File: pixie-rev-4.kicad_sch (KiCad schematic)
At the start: 40 parts, among them J1 THD_FPC_24, SW1 SW_tact_52x52, SW2 SW_tact_52x52, SW3 SW_tact_52x52, SW4 SW_tact_52x52, U1 USBLC6-2SC6, U2 W25Q128JVS, U3 SPX3819M5-L-3-3, U4 ESP32_C3, Y2 Crystal_GND24

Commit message: Check-in before trying ESP32-C3-F4.
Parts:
- U4: footprint Package_DFN_QFN:HVQFN-32-1EP_5x5mm_P0.5mm_EP3.1x3.1mm -> Package_DFN_QFN:QFN-32-1EP_5x5mm_P0.5mm_EP3.7x3.7mm
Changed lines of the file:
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@@
       (effects (font (size 1.27 1.27)) (justify left))
     )
-    (property "Footprint" "Package_DFN_QFN:HVQFN-32-1EP_5x5mm_P0.5mm_EP3.1x3.1mm" (at 166.37 82.55 0)
+    (property "Footprint" "Package_DFN_QFN:QFN-32-1EP_5x5mm_P0.5mm_EP3.7x3.7mm" (at 166.37 82.55 0)
       (effects (font (size 1.27 1.27)) hide)
     )

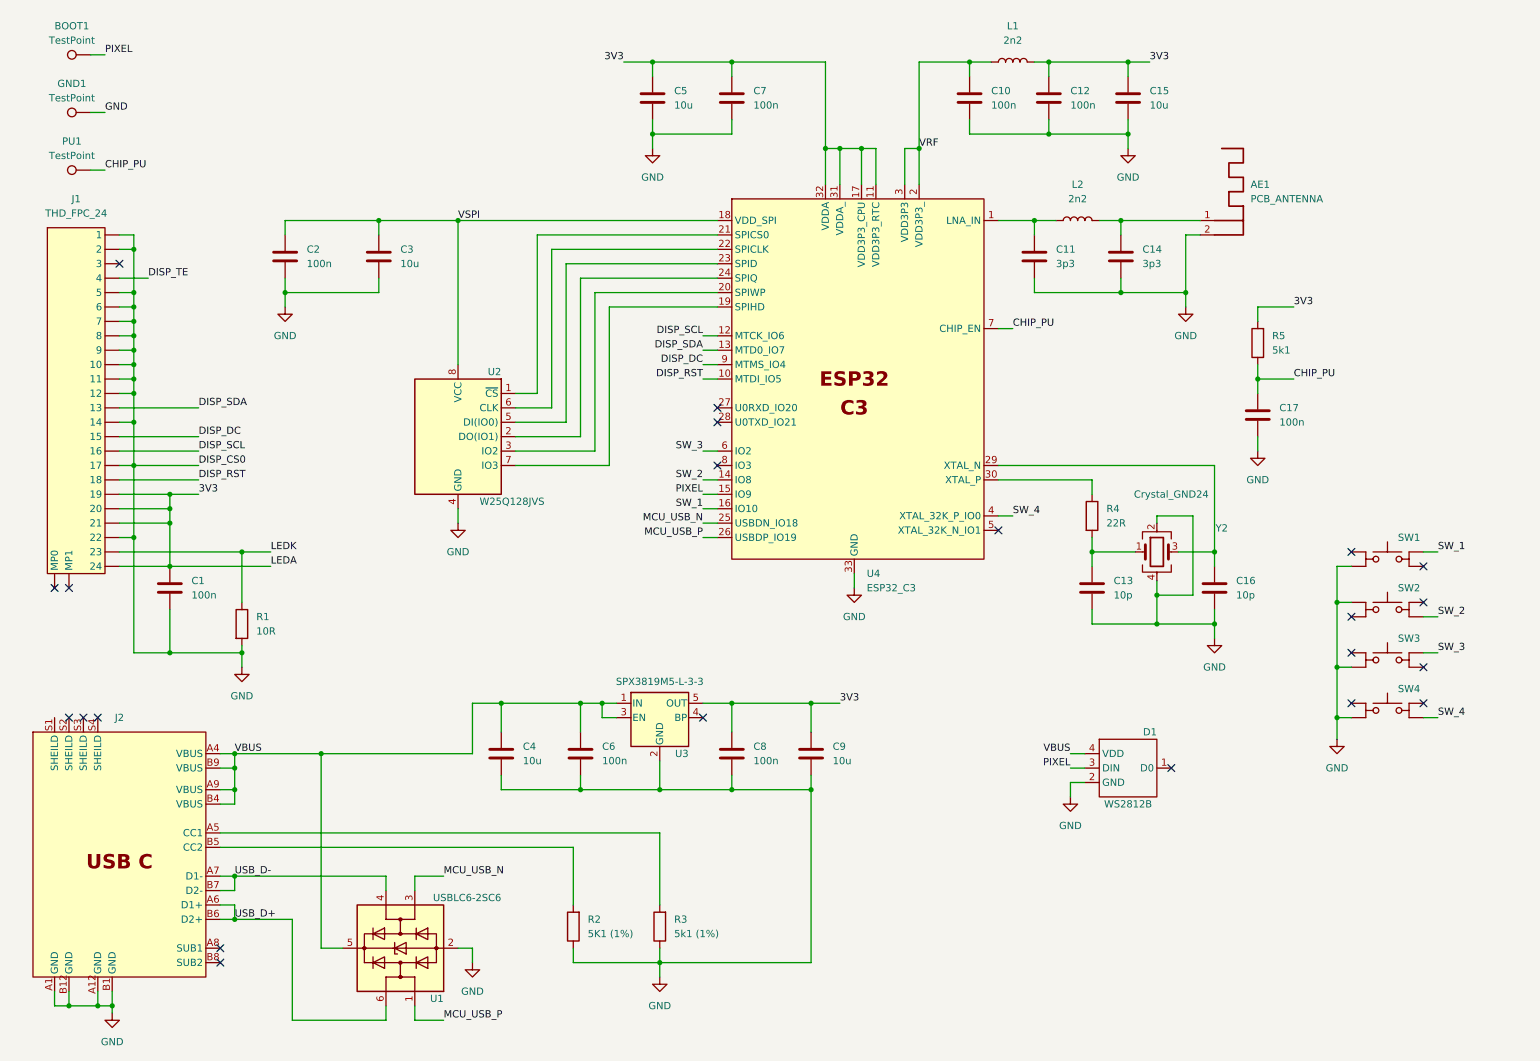
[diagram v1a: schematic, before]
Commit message: Checking in before updating against ESP32-C3-WROOM-02 designs.
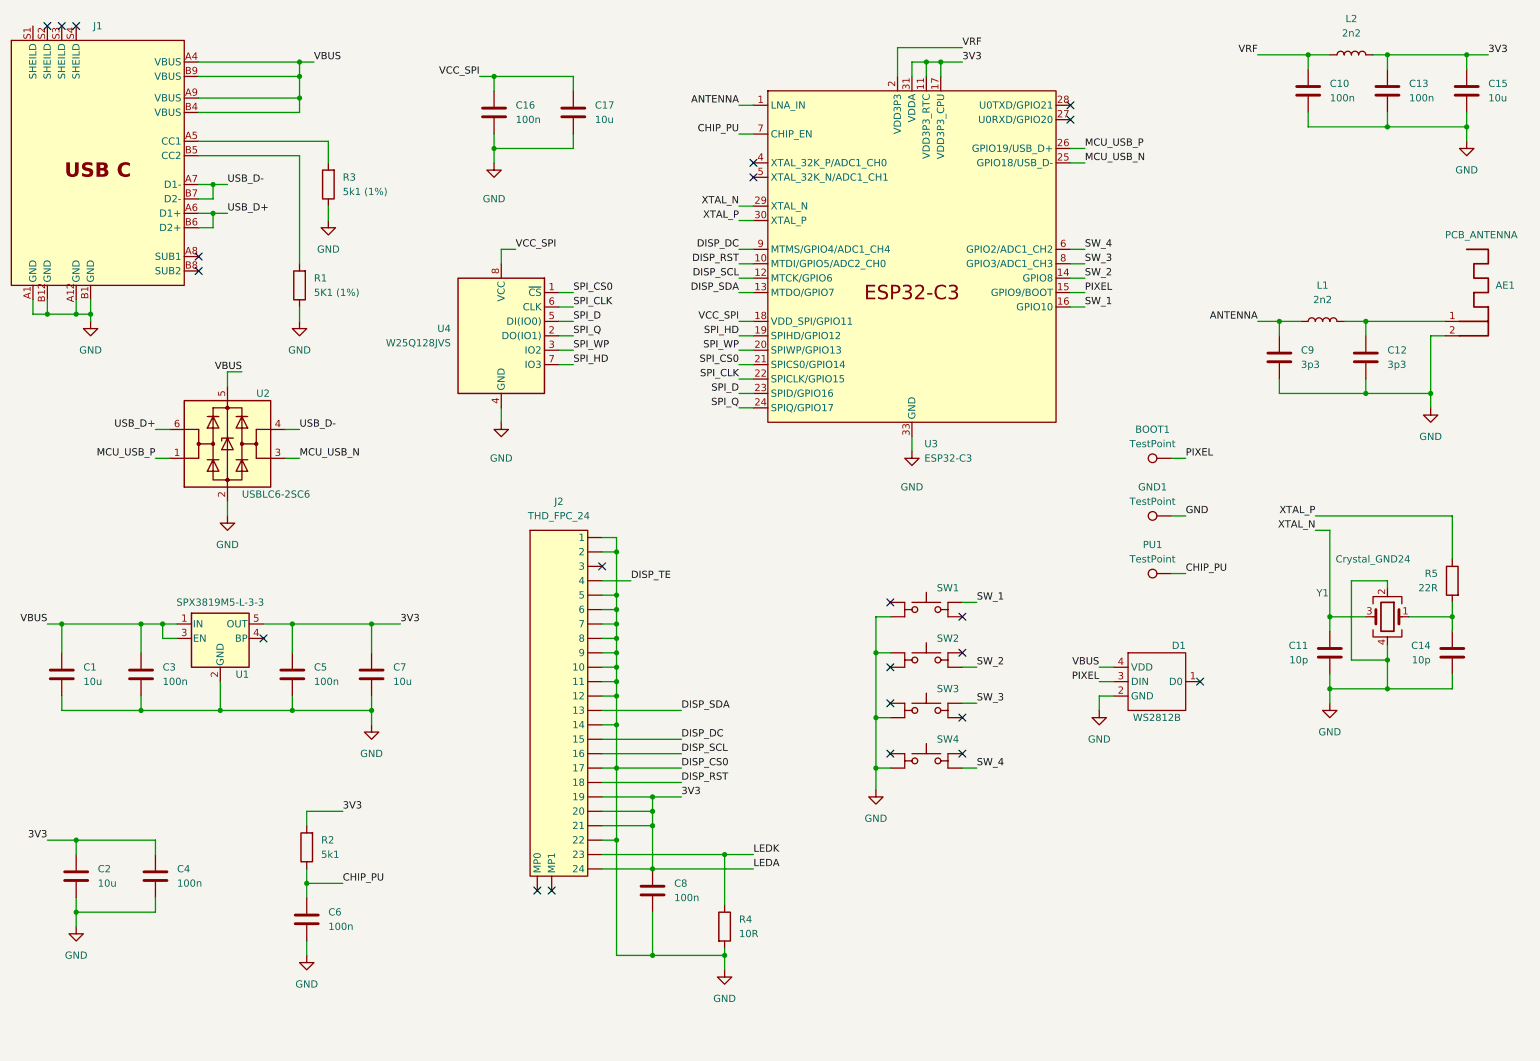
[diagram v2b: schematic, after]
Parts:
- removed C2: 100n, Capacitor_SMD:C_0201_0603Metric, symbol Device:C
- removed C3: 10u, Capacitor_SMD:C_0201_0603Metric, symbol Device:C
- removed U1: USBLC6-2SC6, Package_TO_SOT_SMD:SOT-23-6, symbol Power_Protection:USBLC6-2SC6
- removed U2: W25Q128JVS, Package_SO:SOIC-8_5.23x5.23mm_P1.27mm, symbol Memory_Flash:W25Q128JVS
- removed U4: ESP32_C3, Package_DFN_QFN:QFN-32-1EP_5x5mm_P0.5mm_EP3.7x3.7mm, symbol Firefly:ESP32_C3
- added C16: 100n, Capacitor_SMD:C_0201_0603Metric, symbol Device:C
- added C17: 10u, Capacitor_SMD:C_0201_0603Metric, symbol Device:C
- added U2: USBLC6-2SC6, Package_TO_SOT_SMD:SOT-563, symbol Power_Protection:USBLC6-2SC6
- added U3: ESP32-C3, Package_DFN_QFN:QFN-32-1EP_5x5mm_P0.5mm_EP3.1x3.1mm_ThermalVias, symbol PCM_Espressif:ESP32-C3
- added U4: W25Q128JVS, Package_SO:SOIC-8_5.23x5.23mm_P1.27mm, symbol Memory_Flash:W25Q128JVS
- D1: MPN (none) -> C2976072; Vendor C2976072 -> (none)
- J1: renamed from J2; MPN (none) -> C2906289; Vendor C2906289 -> (none)
- SW1, SW2, SW3, SW4: MPN (none) -> C318884
- U1: renamed from U3; MPN (none) -> C5370980; Vendor C5370980 -> (none)
- Y1: renamed from Y2; MPN (none) -> C255973; Vendor C255973 -> (none)
- renumbered C4 to C1, C16 to C11, C14 to C12, C12 to C13, C13 to C14, C5 to C2, C6 to C3, C7 to C4, C8 to C5, C17 to C6, C9 to C7, C1 to C8, C11 to C9, J1 to J2, L2 to L1, L1 to L2, R2 to R1, R5 to R2, R1 to R4, R4 to R5
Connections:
- net 3V3: now also U3.11 (VDD3P3_RTC), U3.17 (VDD3P3_CPU), U3.31 (VDDA), U3.32 (VDDA)
- net CHIP_PU: now also U3.7 (CHIP_EN)
- net DISP_DC: now also U3.9 (MTMS/GPIO4/ADC1_CH4)
- net DISP_RST: now also U3.10 (MTDI/GPIO5/ADC2_CH0)
- net DISP_SCL: now also U3.12 (MTCK/GPIO6)
- net DISP_SDA: now also U3.13 (MTDO/GPIO7)
- net GND: now also C16.2, C17.2, U2.2 (GND), U3.33 (GND), U4.4 (GND)
- net MCU_USB_N: now also U2.3 (I/O2), U3.25 (GPIO18/USB_D-)
- net MCU_USB_P: now also U2.1 (I/O1), U3.26 (GPIO19/USB_D+)
- net PIXEL: now also U3.15 (GPIO9/BOOT)
- net SW_1: now also U3.16 (GPIO10)
- net SW_2: now also U3.14 (GPIO8)
- net SW_3: now also U3.8 (GPIO3/ADC1_CH3)
- net SW_4: now also U3.6 (GPIO2/ADC1_CH2)
- net USB_D+: now also U2.6 (I/O1)
- net USB_D-: now also U2.4 (I/O2)
- net VBUS: now also U2.5 (VBUS)
- net VRF: now also U3.2 (VDD3P3), U3.3 (VDD3P3)
- net XTAL_P: now reaches R5.1
- net XTAL_P: now also U3.30 (XTAL_P)
- net ANTENNA: now reaches C9.1, L1.1
- net ANTENNA: now also U3.1 (LNA_IN)
- net XTAL_N: now reaches C11.1, Y1.3
- net XTAL_N: now also U3.29 (XTAL_N)
- new net SPI_CLK: U3.22 (SPICLK/GPIO15), U4.6 (CLK)
- new net SPI_CS0: U3.21 (SPICS0/GPIO14), U4.1 (~{CS})
- new net SPI_D: U3.23 (SPID/GPIO16), U4.5 (DI(IO0))
- new net SPI_HD: U3.19 (SPIHD/GPIO12), U4.7 (IO3)
- new net SPI_Q: U3.24 (SPIQ/GPIO17), U4.2 (DO(IO1))
- new net SPI_WP: U3.20 (SPIWP/GPIO13), U4.3 (IO2)
- new net VCC_SPI: C16.1, C17.1, U3.18 (VDD_SPI/GPIO11), U4.8 (VCC)
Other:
- moved on the sheet: AE1, BOOT1, C1, C10, C11, C12, C13, C14, C15, C2, C3, C4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

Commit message: JLCPCB Submit
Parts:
- removed AE1: PCB_ANTENNA, RF_Antenna:Texas_SWRA117D_2.4GHz_Left, symbol Firefly:PCB_ANTENNA
- removed BOOT1, GND1, PU1: TestPoint, TestPoint:TestPoint_Pad_1.5x1.5mm, symbol Connector:TestPoint
- removed C1, C15, C17, C2, C7: 10u, Capacitor_SMD:C_0201_0603Metric, symbol Device:C
- removed C10, C13, C16, C3, C4, C5, C6, C8: 100n, Capacitor_SMD:C_0201_0603Metric, symbol Device:C
- removed C11, C14: 10p, Capacitor_SMD:C_0201_0603Metric, symbol Device:C
- removed C12, C9: 3p3, Capacitor_SMD:C_0201_0603Metric, symbol Device:C
- removed D1: WS2812B, firefly:WS2812B, symbol firefly:WS2812B
- removed J1: ~, firefly:USB_C_SINK, symbol Firefly:USB_C_SINK
- removed J2: THD_FPC_24, firefly:THD_FPC_24, symbol firefly:THD_FPC_24
- removed L1, L2: 2n2, Inductor_SMD:L_0201_0603Metric, symbol Device:L
- removed R1: 5K1 (1%), Resistor_SMD:R_0201_0603Metric, symbol Device:R
- removed R2: 5k1, Resistor_SMD:R_0201_0603Metric, symbol Device:R
- removed R3: 5k1 (1%), Resistor_SMD:R_0201_0603Metric, symbol Device:R
- removed R4: 10R, Resistor_SMD:R_0201_0603Metric, symbol Device:R
- removed R5: 22R, Resistor_SMD:R_0201_0603Metric, symbol Device:R
- removed SW1, SW2, SW3, SW4: SW_tact_52x52, firefly:SW_tact_52x52, symbol firefly:SW_tact_52x52
- removed U1: SPX3819M5-L-3-3, Package_TO_SOT_SMD:SOT-23-5, symbol Regulator_Linear:SPX3819M5-L-3-3
- removed U2: USBLC6-2SC6, Package_TO_SOT_SMD:SOT-563, symbol Power_Protection:USBLC6-2SC6
- removed U3: ESP32-C3, Package_DFN_QFN:QFN-32-1EP_5x5mm_P0.5mm_EP3.1x3.1mm_ThermalVias, symbol PCM_Espressif:ESP32-C3
- removed U4: W25Q128JVS, Package_SO:SOIC-8_5.23x5.23mm_P1.27mm, symbol Memory_Flash:W25Q128JVS
- removed Y1: Crystal_GND24, firefly:Crystal_SeikoEpson_FA20H, symbol Device:Crystal_GND24
- added SW101, SW102, SW103, SW104: SW_tact_52x52, firefly:SW_tact_52x52, symbol firefly:SW_tact_52x52
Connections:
- net GND: now also SW101.1, SW101.3, SW102.1, SW102.3, SW103.1, SW103.3, SW104.1, SW104.3
- net SW_1: now also SW101.2
- net SW_2: now also SW102.4
- net SW_3: now also SW103.2
- net SW_4: now also SW104.4
- no-connect marks 22 -> 4
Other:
- added sheet MCU (mcu.kicad_sch)
- added sheet Output (output.kicad_sch)
- added sheet Power (power.kicad_sch)
- note added: "Exports globals: - 3v3 - 5v"
- title: (none) -> Firefly Pixie

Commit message: Checking in before submitting rev.5 to JLCPCB.
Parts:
- removed SW101, SW102, SW103, SW104: SW_tact_52x52, firefly:SW_tact_52x52, symbol firefly:SW_tact_52x52
- added SW1, SW2, SW3, SW4: ~, firefly:button-oval, symbol Firefly:SW_12_34
- added TP1, TP2: TestPoint, TestPoint:TestPoint_Pad_D1.0mm, symbol Connector:TestPoint
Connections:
- net GND: now also SW1.1, SW1.2, SW2.1, SW2.2, SW3.1, SW3.2, SW4.1, SW4.2
- net SW_3: now also SW3.3
- net SW_4: now also SW4.3
- new net MCU/IO20: TP1.1
- new net MCU/IO21: TP2.1
- new net MCU/SW_1: SW1.4
- new net MCU/SW_2: SW2.4
- no-connect marks 4 -> 0
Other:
- sheet MCU ports: added IO20, IO21; removed none
